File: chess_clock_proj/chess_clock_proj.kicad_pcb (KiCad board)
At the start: 2 copper layers, 146.5 x 73.4 mm, 40 parts, among them J1 USB_A, J2 Conn_01x04_Male, J3 Conn_01x04_Male, J4 Conn_01x02, SW1 SW_SPDT, SW2 SW_Push, SW3 SW_Push, SW4 SW_Push, SW5 SW_Push, SW6 SW_Push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

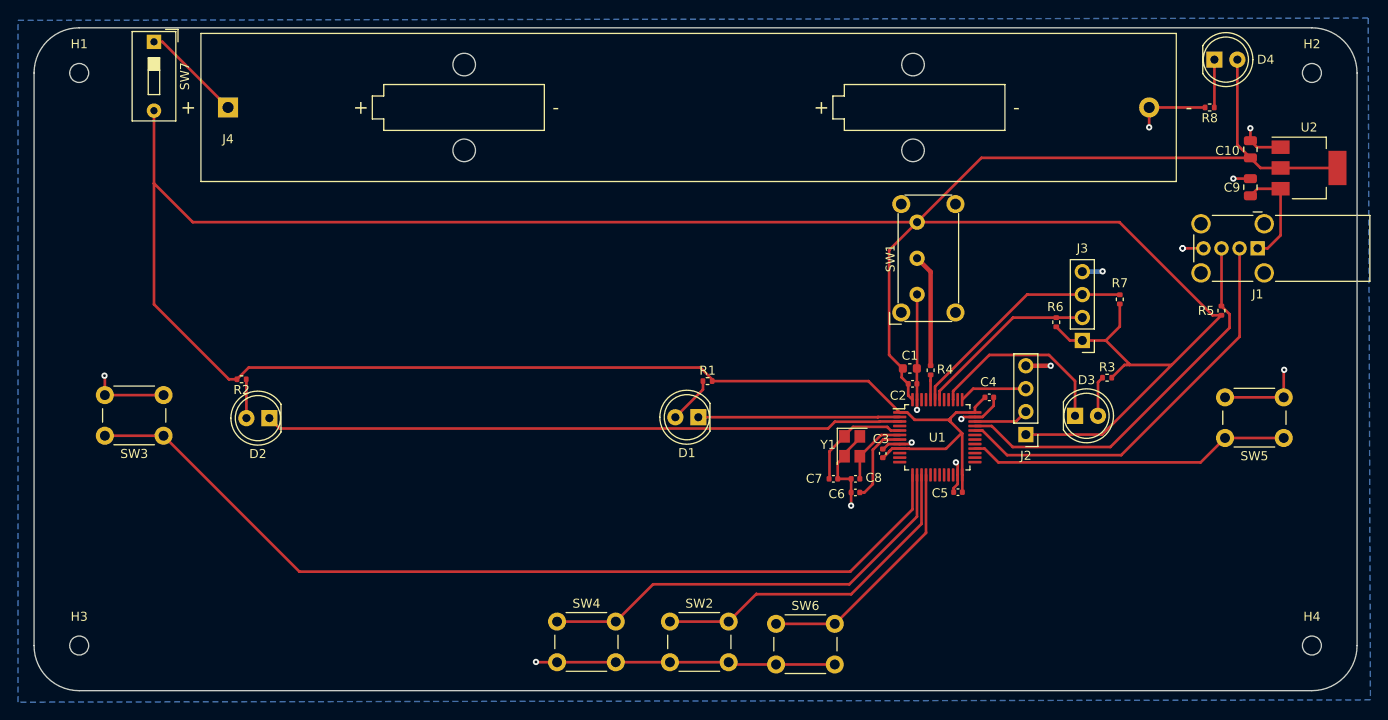
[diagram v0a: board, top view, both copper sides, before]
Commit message: alterei a posição da malha de terra, e retirei o resistor próximo ao USB
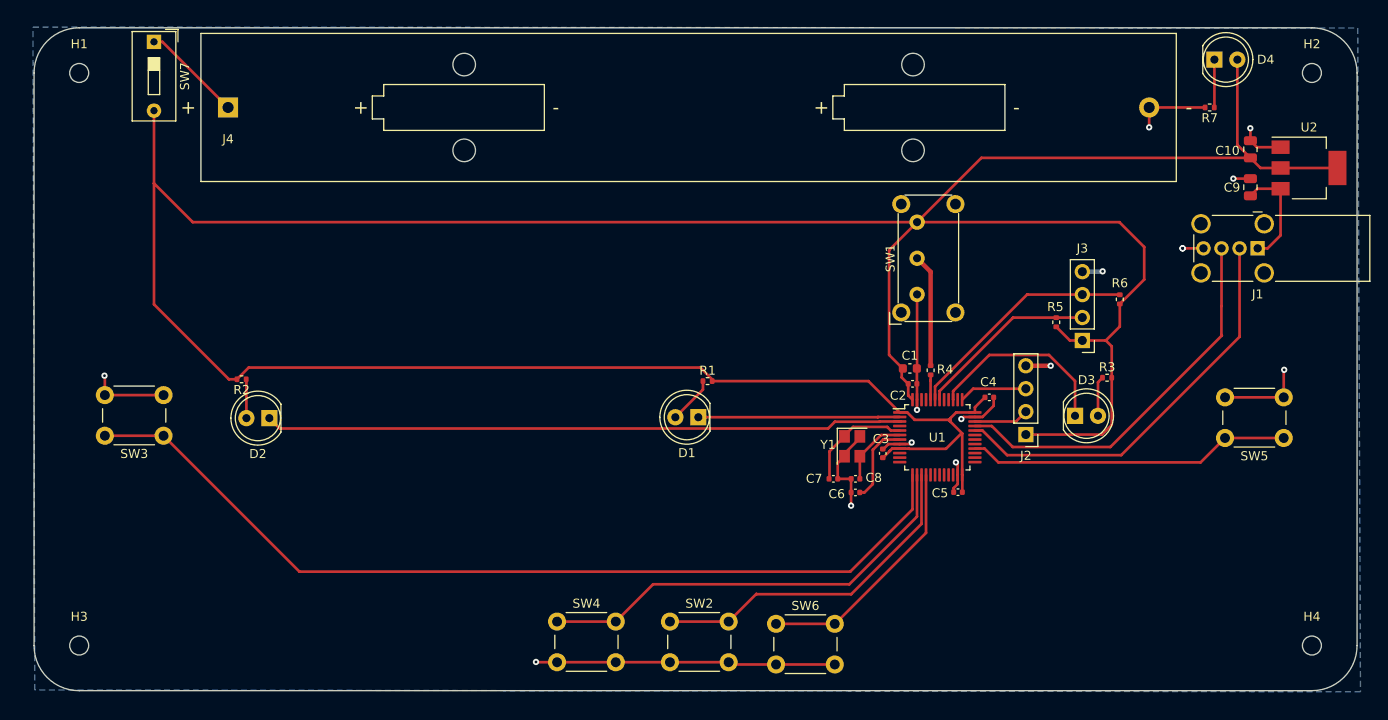
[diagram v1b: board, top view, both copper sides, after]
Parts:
- removed the R5 at (206.5, 88.9)
- renumbered R6 to R5, R7 to R6, R8 to R7
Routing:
- net +3V3: track 396.9 -> 374.1 mm
- net /USB_D+: track 43.8 -> 43.1 mm
